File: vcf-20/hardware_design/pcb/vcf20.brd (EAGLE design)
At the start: 30 x 100 mm, 59 parts, among them IC1 LM13700M, J1 WQP-PJ301M-12_JACK, J2 WQP-PJ301M-12_JACK, J3 WQP-PJ301M-12_JACK, J4 WQP-PJ301M-12_JACK, T1 3904, T2 3904, U1 TL072AD, U2 TL072AD, U3 NE5532D

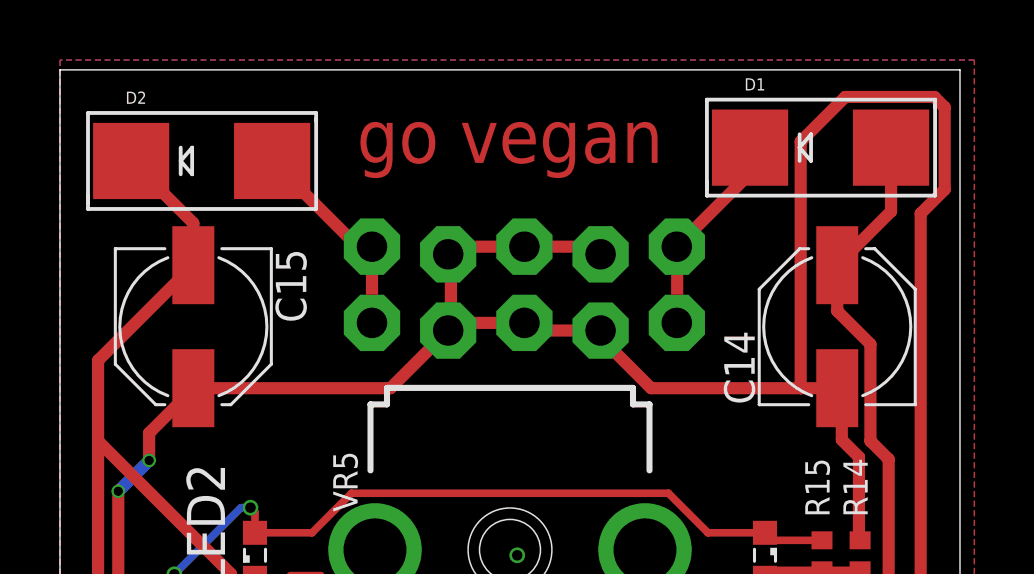
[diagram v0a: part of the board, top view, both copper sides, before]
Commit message: Fix reversed power connector for vcf-20
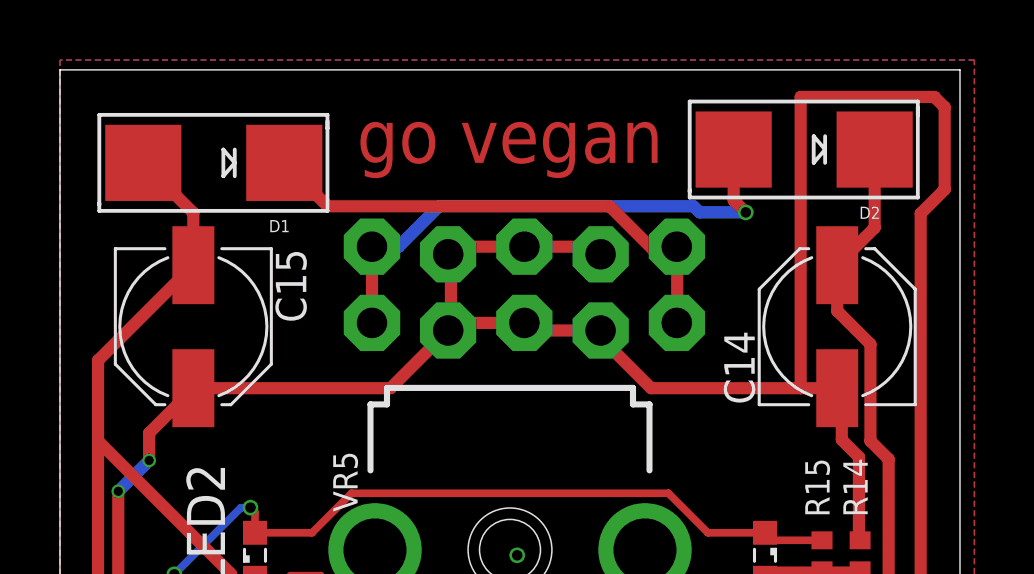
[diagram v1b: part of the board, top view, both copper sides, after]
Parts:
- T1, T2: value 3904 -> 3906
- moved D1 20.2 mm to (5.13, 96.9), turned to 180 degrees
- moved D2 20.1 mm to (24.8, 97.3), turned to 180 degrees
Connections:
- net +12V: now also D2.C; no longer D1.A
- net -12V: now also D1.A; no longer D2.C
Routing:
- net N$30: track 7.05 -> 18.4 mm, vias 0 -> 1
- net N$33: track 6.86 -> 16.8 mm
- net GND: track 284.3 -> 285.1 mm
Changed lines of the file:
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@@
 <drawing>
 <settings>
-<setting alwaysvectorfont="yes"/>
+<setting alwaysvectorfont="no"/>
 <setting verticaltext="up"/>
 </settings>
@@
 <attribute name="VALUE" x="15.24" y="70.485" size="0.8128" layer="27" font="vector"/>
 </element>
-<element name="T1" library="transistor" library_urn="urn:adsk.eagle:library:402" package="SOT23-BEC" package3d_urn="urn:adsk.eagle:package:28748/2" value="3904" x="15.5575" y="33.655" smashed="yes">
+<element name="T1" library="transistor" library_urn="urn:adsk.eagle:library:402" package="SOT23-BEC" package3d_urn="urn:adsk.eagle:package:28748/2" value="3906" x="15.5575" y="33.655" smashed="yes">
 <attribute name="NAME" x="14.2875" y="30.48" size="1.27" layer="25"/>
 <attribute name="POPULARITY" value="0" x="15.5575" y="33.655" size="1.778" layer="27" display="off"/>
 <attribute name="VALUE" x="13.6525" y="30.48" size="1.27" layer="27"/>
 </element>
-<element name="T2" library="transistor" library_urn="urn:adsk.eagle:library:402" package="SOT23-BEC" package3d_urn="urn:adsk.eagle:package:28748/2" value="3904" x="19.685" y="33.655" smashed="yes">
+<element name="T2" library="transistor" library_urn="urn:adsk.eagle:library:402" package="SOT23-BEC" package3d_urn="urn:adsk.eagle:package:28748/2" value="3906" x="19.685" y="33.655" smashed="yes">
 <attribute name="NAME" x="21.59" y="33.02" size="1.27" layer="25"/>
 <attribute name="POPULARITY" value="0" x="19.685" y="33.655" size="1.778" layer="27" display="off"/>
@@
 <attribute name="VALUE" x="17.145" y="67.183" size="0.8128" layer="27" font="vector"/>
 </element>
-<element name="D1" library="adafruit" library_urn="urn:adsk.eagle:library:420" package="SMADIODE" package3d_urn="urn:adsk.eagle:package:6240747/1" value="1N4001" x="25.353" y="97.409" smashed="yes">
-<attribute name="NAME" x="22.813" y="99.314" size="0.4064" layer="25" font="vector"/>
-<attribute name="VALUE" x="22.813" y="95.123" size="0.4064" layer="27" font="vector"/>
-</element>
-<element name="D2" library="adafruit" library_urn="urn:adsk.eagle:library:420" package="SMADIODE" package3d_urn="urn:adsk.eagle:package:6240747/1" value="1N4001" x="4.722" y="96.9645" smashed="yes">
-<attribute name="NAME" x="2.182" y="98.8695" size="0.4064" layer="25" font="vector"/>
-<attribute name="VALUE" x="2.182" y="94.6785" size="0.4064" layer="27" font="vector"/>
+<element name="D1" library="adafruit" library_urn="urn:adsk.eagle:library:420" package="SMADIODE" package3d_urn="urn:adsk.eagle:package:6240747/1" value="1N4001" x="5.127" y="96.901" smashed="yes" rot="R180">
+<attribute name="NAME" x="7.667" y="94.996" size="0.4064" layer="25" font="vector" rot="R180"/>
+<attribute name="VALUE" x="7.667" y="99.187" size="0.4064" layer="27" font="vector" rot="R180"/>
+</element>
+<element name="D2" library="adafruit" library_urn="urn:adsk.eagle:library:420" package="SMADIODE" package3d_urn="urn:adsk.eagle:package:6240747/1" value="1N4001" x="24.8055" y="97.3455" smashed="yes" rot="R180">
+<attribute name="NAME" x="27.3455" y="95.4405" size="0.4064" layer="25" font="vector" rot="R180"/>
+<attribute name="VALUE" x="27.3455" y="99.6315" size="0.4064" layer="27" font="vector" rot="R180"/>
 </element>
 <element name="C14" library="rcl" library_urn="urn:adsk.eagle:library:334" package="PANASONIC_C" package3d_urn="urn:adsk.eagle:package:23422/2" value="10uF" x="25.908" y="91.44" smashed="yes" rot="R90">
@@
 <wire x1="29.4894" y1="98.7552" x2="29.4894" y2="96.012" width="0.4064" layer="1"/>
 <wire x1="29.1465" y1="99.0981" x2="29.4894" y2="98.7552" width="0.4064" layer="1"/>
-<wire x1="26.1747" y1="99.0981" x2="29.1465" y2="99.0981" width="0.4064" layer="1"/>
-<wire x1="24.6888" y1="97.6122" x2="26.1747" y2="99.0981" width="0.4064" layer="1"/>
-<wire x1="24.6888" y1="89.39" x2="24.6888" y2="97.6122" width="0.4064" layer="1"/>
+<wire x1="24.6888" y1="99.0981" x2="29.1465" y2="99.0981" width="0.4064" layer="1"/>
+<wire x1="24.6888" y1="89.39" x2="24.6888" y2="99.0981" width="0.4064" layer="1"/>
 <wire x1="28.6893" y1="74.295" x2="28.59" y2="74.295" width="0.4064" layer="1"/>
 <wire x1="5.6007" y1="80.9244" x2="6.5151" y2="80.01" width="0.4064" layer="1"/>
@@
 <contactref element="C4" pad="1"/>
 <contactref element="C5" pad="1"/>
-<contactref element="D1" pad="A"/>
 <contactref element="C14" pad="+"/>
 <contactref element="U1" pad="8"/>
@@
 <contactref element="U3" pad="8"/>
 <contactref element="IC1" pad="11"/>
-<wire x1="27.7025" y1="97.409" x2="27.7025" y2="95.2845" width="0.4064" layer="1"/>
-<wire x1="27.7025" y1="95.2845" x2="25.908" y2="93.49" width="0.4064" layer="1"/>
 <wire x1="25.908" y1="93.49" x2="25.908" y2="91.9647375" width="0.4064" layer="1"/>
 <wire x1="25.908" y1="91.9647375" x2="27.0144" y2="90.8583375" width="0.4064" layer="1"/>
@@
 <wire x1="24.585" y1="77" x2="17.5" y2="77" width="0.4064" layer="1"/>
 <wire x1="27.29" y1="74.295" x2="24.585" y2="77" width="0.4064" layer="1"/>
+<contactref element="D2" pad="C"/>
+<wire x1="25.908" y1="93.49" x2="27.155" y2="94.737" width="0.4064" layer="1"/>
+<wire x1="27.155" y1="94.737" x2="27.155" y2="97.3455" width="0.4064" layer="1"/>
 </signal>
 <signal name="-12V" class="1">
@@
 <contactref element="C11" pad="2"/>
 <contactref element="C12" pad="2"/>
-<contactref element="D2" pad="C"/>
 <contactref element="C15" pad="-"/>
 <contactref element="U1" pad="4"/>
@@
 <contactref element="U3" pad="4"/>
 <contactref element="IC1" pad="6"/>
-<wire x1="2.3725" y1="96.9645" x2="4.445" y2="94.892" width="0.4064" layer="1"/>
-<wire x1="4.445" y1="94.892" x2="4.445" y2="93.49" width="0.4064" layer="1"/>
 <wire x1="4.445" y1="93.49" x2="1.27" y2="90.315" width="0.4064" layer="1"/>
 <wire x1="1.27" y1="90.315" x2="1.27" y2="87.63" width="0.4064" layer="1"/>
@@
 <wire x1="5.6936" y1="82.5016625" x2="5.9627625" y2="82.2325" width="0.4064" layer="1"/>
 <wire x1="5.9627625" y1="82.2325" x2="7.2675" y2="82.2325" width="0.4064" layer="1"/>
+<contactref element="D1" pad="A"/>
+<wire x1="4.445" y1="95.2335" x2="2.7775" y2="96.901" width="0.4064" layer="1"/>
+<wire x1="4.445" y1="93.49" x2="4.445" y2="95.2335" width="0.4064" layer="1"/>
 </signal>
 <signal name="N$25">
@@
 <contactref element="D2" pad="A"/>
 <wire x1="10.4" y1="94.107" x2="9.929" y2="94.107" width="0.4064" layer="1"/>
-<wire x1="9.929" y1="94.107" x2="7.0715" y2="96.9645" width="0.4064" layer="1"/>
 <wire x1="10.4" y1="94.107" x2="10.4" y2="91.567" width="0.4064" layer="1"/>
+<via x="22.86" y="95.25" extent="1-16" drill="0.35"/>
+<wire x1="10.4" y1="94.107" x2="11.29018125" y2="94.107" width="0.4064" layer="16"/>
+<wire x1="21.11761875" y1="95.4532" x2="21.32081875" y2="95.25" width="0.4064" layer="16"/>
+<wire x1="21.32081875" y1="95.25" x2="22.86" y2="95.25" width="0.4064" layer="16"/>
+<wire x1="11.29018125" y1="94.107" x2="12.63638125" y2="95.4532" width="0.4064" layer="16"/>
+<wire x1="12.63638125" y1="95.4532" x2="21.11761875" y2="95.4532" width="0.4064" layer="16"/>
+<wire x1="22.86" y1="95.25" x2="22.456" y2="95.654" width="0.4064" layer="1"/>
+<wire x1="22.456" y1="95.654" x2="22.456" y2="97.3455" width="0.4064" layer="1"/>
 </signal>
 <signal name="N$33" class="1">
@@
 <contactref element="C9" pad="NEG1"/>
 <contactref element="D1" pad="C"/>
-<wire x1="20.56" y1="94.107" x2="23.0035" y2="96.5505" width="0.4064" layer="1"/>
-<wire x1="23.0035" y1="96.5505" x2="23.0035" y2="97.409" width="0.4064" layer="1"/>
 <wire x1="20.574" y1="93.9546" x2="20.574" y2="91.6686" width="0.4064" layer="1"/>
 <wire x1="20.574" y1="91.6686" x2="20.56" y2="91.567" width="0.4064" layer="1"/>
-<wire x1="20.574" y1="93.9546" x2="20.56" y2="94.107" width="0.4064" layer="1"/>
+<wire x1="20.574" y1="93.9546" x2="20.569559375" y2="94.002925" width="0.4064" layer="1"/>
+<wire x1="20.569559375" y1="94.002925" x2="20.56" y2="94.107" width="0.4064" layer="1"/>
+<wire x1="7.4765" y1="96.901" x2="8.9243" y2="95.4532" width="0.4064" layer="1"/>
+<wire x1="19.77389375" y1="94.002925" x2="20.569559375" y2="94.002925" width="0.4064" layer="1"/>
+<wire x1="18.32361875" y1="95.4532" x2="19.77389375" y2="94.002925" width="0.4064" layer="1"/>
+<wire x1="8.9243" y1="95.4532" x2="18.32361875" y2="95.4532" width="0.4064" layer="1"/>
 </signal>
 </signals>
